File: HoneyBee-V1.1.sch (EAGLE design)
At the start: 47 parts, among them IC2 CA3130EZLMP, Q1 2N5457

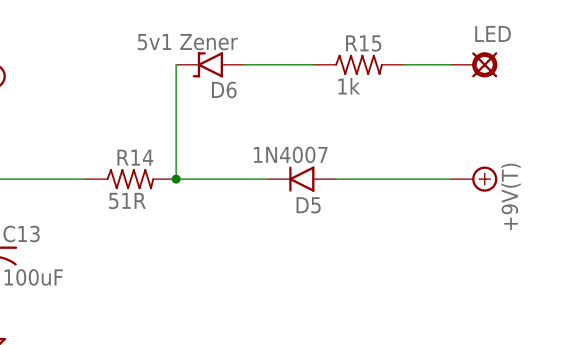
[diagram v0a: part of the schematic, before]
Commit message: Changes to layout and schematic.
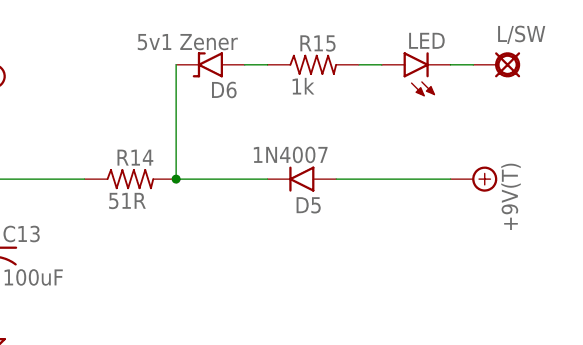
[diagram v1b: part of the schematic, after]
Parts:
- added L/SW: (no value), mb_supply:PAD
- LED: device mb_supply:PAD -> mb_diodes:LED3MM
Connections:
- new net N$20: LED.A, R15.2
- net N$25: now also L/SW.PAD, LED.C; no longer LED.PAD, R15.2
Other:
- moved on the sheet: R15
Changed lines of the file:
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@@
 <part name="D5" library="mb_diodes" deviceset="1N400X" device=".3" value="1N4007"/>
 <part name="D6" library="mb_diodes" deviceset="1N9*ZENER" device="" value="5v1 Zener"/>
-<part name="LED" library="mb_supply" deviceset="PAD" device="" value="3mm"/>
+<part name="LED" library="mb_diodes" deviceset="LED" device="3MM" value="3mm"/>
 <part name="C13" library="mb_caps-electro" deviceset="080" device="1" value="100uF"/>
 <part name="GND13" library="mb_supply" deviceset="GND" device=""/>
@@
 <part name="GND1" library="mb_supply" deviceset="GND" device=""/>
 <part name="GND6" library="mb_supply" deviceset="GND" device=""/>
+<part name="L/SW" library="mb_supply" deviceset="PAD" device=""/>
 </parts>
 <sheets>
@@
 <instance part="R13" gate="G$1" x="195.58" y="101.6"/>
 <instance part="R14" gate="G$1" x="185.42" y="132.08"/>
-<instance part="R15" gate="G$1" x="210.82" y="144.78"/>
+<instance part="R15" gate="G$1" x="205.74" y="144.78"/>
 <instance part="C1" gate="G$1" x="27.94" y="96.52" rot="R90"/>
 <instance part="C2" gate="G$1" x="73.66" y="101.6" rot="R90"/>
@@
 <instance part="D5" gate="1" x="203.2" y="132.08" rot="R180"/>
 <instance part="D6" gate="G$1" x="195.58" y="144.78" rot="R180"/>
-<instance part="LED" gate="G$1" x="223.52" y="144.78"/>
+<instance part="LED" gate="G$1" x="218.44" y="144.78" rot="R180"/>
 <instance part="C13" gate="G$1" x="170.18" y="124.46"/>
 <instance part="GND13" gate="GND" x="213.36" y="76.2"/>
@@
 <instance part="GND1" gate="GND" x="129.54" y="111.76"/>
 <instance part="GND6" gate="GND" x="139.7" y="111.76"/>
+<instance part="L/SW" gate="G$1" x="226.06" y="144.78"/>
 </instances>
 <busses>
@@
 <pinref part="D6" gate="G$1" pin="A"/>
 <pinref part="R15" gate="G$1" pin="1"/>
-<wire x1="198.12" y1="144.78" x2="205.74" y2="144.78" width="0.1524" layer="91"/>
-</segment>
-</net>
-<net name="N$25" class="0">
-<segment>
-<pinref part="R15" gate="G$1" pin="2"/>
-<pinref part="LED" gate="G$1" pin="PAD"/>
-<wire x1="215.9" y1="144.78" x2="220.98" y2="144.78" width="0.1524" layer="91"/>
+<wire x1="198.12" y1="144.78" x2="200.66" y2="144.78" width="0.1524" layer="91"/>
 </segment>
 </net>
@@
 </segment>
 </net>
+<net name="N$20" class="0">
+<segment>
+<pinref part="R15" gate="G$1" pin="2"/>
+<pinref part="LED" gate="G$1" pin="A"/>
+<wire x1="213.36" y1="144.78" x2="210.82" y2="144.78" width="0.1524" layer="91"/>
+</segment>
+</net>
+<net name="N$25" class="0">
+<segment>
+<pinref part="LED" gate="G$1" pin="C"/>
+<pinref part="L/SW" gate="G$1" pin="PAD"/>
+<wire x1="223.52" y1="144.78" x2="220.98" y2="144.78" width="0.1524" layer="91"/>
+</segment>
+</net>
